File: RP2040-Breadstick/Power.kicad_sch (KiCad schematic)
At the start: 11 parts, among them IC501 LM66200DRLR, U501 AP2112K-3.3TRG1

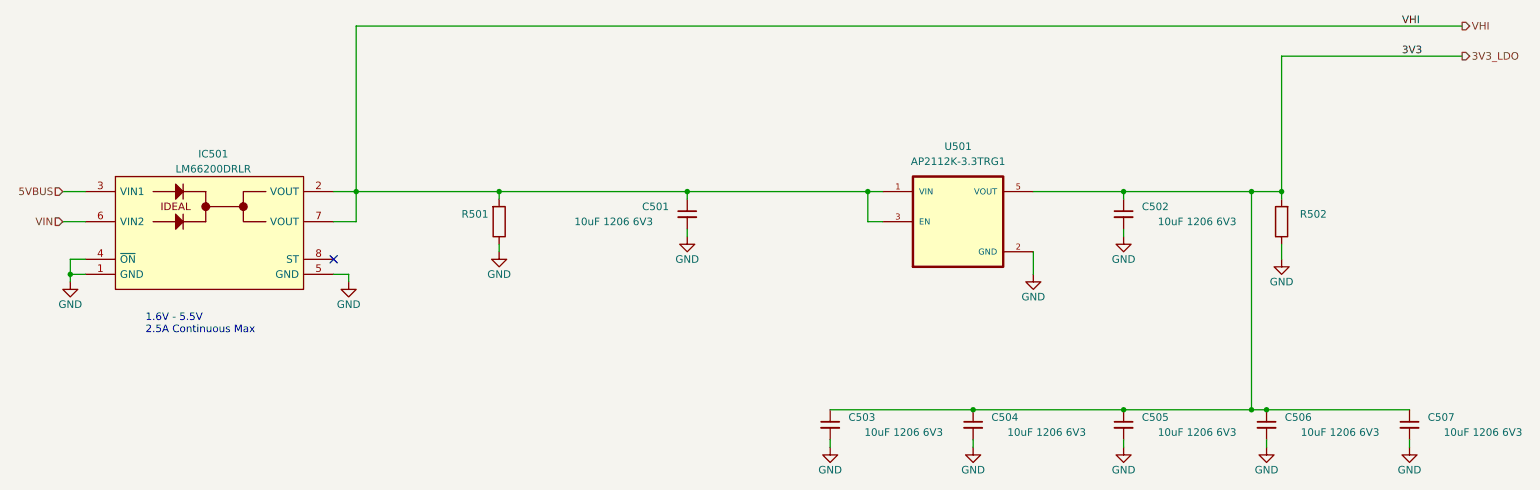
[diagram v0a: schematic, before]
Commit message: Rough routing complete, time to polish it a bit
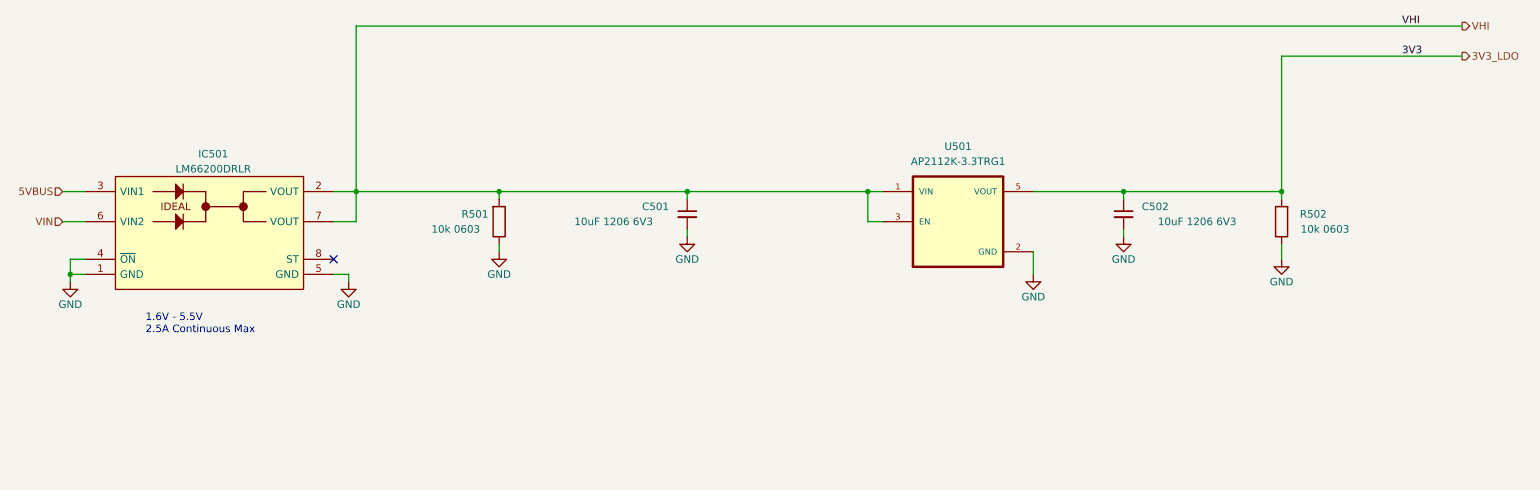
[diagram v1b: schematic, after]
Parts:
- removed C503, C504, C505, C506, C507: 10uF 1206 6V3, Capacitor_SMD:C_1206_3216Metric, symbol Device:C_Small
- R501: value (none) -> 10k 0603; footprint (none) -> Resistor_SMD:R_0603_1608Metric
- R502: value (none) -> 10k 0603

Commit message: Updated BOM
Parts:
- C501, C502: value 10uF 1206 6V3 -> (none); footprint Capacitor_SMD:C_1206_3216Metric -> (none)
- IC501: value LM66200DRLR -> (none); footprint SOTFL50P160X60-8L -> (none); Digikey (none) -> 296-LM66200DRLRCT-ND; Manufacturer (none) -> Texas Instruments; Mouser (none) -> 595-LM66200DRLR
- R501, R502: value 10k 0603 -> (none); footprint Resistor_SMD:R_0603_1608Metric -> (none)
- U501: value AP2112K-3.3TRG1 -> (none); footprint AP2112K-3:SOT95P285X140-5N -> (none); DigiKey_Part_Number AP2112K-3.3TRG1DITR-ND -> (none); Digikey (none) -> AP2112K-3.3TRG1DICT-ND; Manufacturer (none) -> Diodes Incorporated; Manufacturer_Part_Number (none) -> AP2112K-3.3TRG1; Mouser (none) -> 621-AP2112K-3.3TRG1; Package SOT-753 Diodes Inc. -> SOT-25
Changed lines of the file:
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@@
       (effects (font (size 1.27 1.27)) (justify left))
     )
-    (property "Value" "10k 0603" (id 1) (at 245.11 82.55 0)
-      (effects (font (size 1.27 1.27)) (justify left))
-    )
-    (property "Footprint" "Resistor_SMD:R_0603_1608Metric" (id 2) (at 235.458 81.28 90)
+    (property "Value" "" (id 1) (at 245.11 82.55 0)
+      (effects (font (size 1.27 1.27)) (justify left))
+    )
+    (property "Footprint" "" (id 2) (at 235.458 81.28 90)
       (effects (font (size 1.27 1.27)) hide)
     )
@@
       (effects (font (size 1.27 1.27)) (justify left))
     )
-    (property "Value" "10uF 1206 6V3" (id 1) (at 226.06 81.28 0)
-      (effects (font (size 1.27 1.27)) (justify left))
-    )
-    (property "Footprint" "Capacitor_SMD:C_1206_3216Metric" (id 2) (at 207.01 80.01 0)
+    (property "Value" "" (id 1) (at 226.06 81.28 0)
+      (effects (font (size 1.27 1.27)) (justify left))
+    )
+    (property "Footprint" "" (id 2) (at 207.01 80.01 0)
       (effects (font (size 1.27 1.27)) hide)
     )
@@
     (in_bom yes) (on_board yes)
     (property "Reference" "IC501" (id 0) (at 53.34 69.85 0))
-    (property "Value" "LM66200DRLR" (id 1) (at 53.34 72.39 0))
-    (property "Footprint" "SOTFL50P160X60-8L" (id 2) (at 82.55 81.28 0)
+    (property "Value" "" (id 1) (at 53.34 72.39 0))
+    (property "Footprint" "" (id 2) (at 82.55 81.28 0)
       (effects (font (size 1.27 1.27)) (justify left) hide)
     )
@@
     (property "Manufacturer_Part_Number" "LM66200DRLR" (id 9) (at 82.55 99.06 0)
       (effects (font (size 1.27 1.27)) (justify left) hide)
+    )
+    (property "Manufacturer" "Texas Instruments" (id 10) (at 53.34 83.82 0)
+      (effects (font (size 1.27 1.27)) hide)
+    )
+    (property "Digikey" "296-LM66200DRLRCT-ND" (id 11) (at 53.34 83.82 0)
+      (effects (font (size 1.27 1.27)) hide)
+    )
+    (property "Mouser" "595-LM66200DRLR" (id 12) (at 53.34 83.82 0)
+      (effects (font (size 1.27 1.27)) hide)
     )
     (pin "1")
@@
       (effects (font (size 1.27 1.27)) (justify left))
     )
-    (property "Value" "10uF 1206 6V3" (id 1) (at 114.3 81.28 0)
-      (effects (font (size 1.27 1.27)) (justify left))
-    )
-    (property "Footprint" "Capacitor_SMD:C_1206_3216Metric" (id 2) (at 133.35 80.01 0)
+    (property "Value" "" (id 1) (at 114.3 81.28 0)
+      (effects (font (size 1.27 1.27)) (justify left))
+    )
+    (property "Footprint" "" (id 2) (at 133.35 80.01 0)
       (effects (font (size 1.27 1.27)) hide)
     )
@@
     (in_bom yes) (on_board yes) (fields_autoplaced)
     (property "Reference" "U501" (id 0) (at 179.07 68.58 0))
-    (property "Value" "AP2112K-3.3TRG1" (id 1) (at 179.07 71.12 0))
-    (property "Footprint" "AP2112K-3:SOT95P285X140-5N" (id 2) (at 179.07 81.28 0)
+    (property "Value" "" (id 1) (at 179.07 71.12 0))
+    (property "Footprint" "" (id 2) (at 179.07 81.28 0)
       (effects (font (size 1.27 1.27)) (justify bottom) hide)
     )
@@
       (effects (font (size 1.27 1.27)) hide)
     )
-    (property "DigiKey_Part_Number" "AP2112K-3.3TRG1DITR-ND" (id 4) (at 179.07 81.28 0)
+    (property "DigiKey_Part_Number" "" (id 4) (at 179.07 81.28 0)
       (effects (font (size 1.27 1.27)) (justify bottom) hide)
     )
@@
       (effects (font (size 1.27 1.27)) (justify bottom) hide)
     )
-    (property "Package" "SOT-753 Diodes Inc." (id 7) (at 179.07 81.28 0)
+    (property "Package" "SOT-25" (id 7) (at 179.07 81.28 0)
       (effects (font (size 1.27 1.27)) (justify bottom) hide)
     )
@@
     (property "MANUFACTURER" "Diodes Inc." (id 13) (at 179.07 81.28 0)
       (effects (font (size 1.27 1.27)) (justify bottom) hide)
+    )
+    (property "Digikey" "AP2112K-3.3TRG1DICT-ND" (id 14) (at 179.07 81.28 0)
+      (effects (font (size 1.27 1.27)) hide)
+    )
+    (property "Manufacturer" "Diodes Incorporated" (id 15) (at 179.07 81.28 0)
+      (effects (font (size 1.27 1.27)) hide)
+    )
+    (property "Manufacturer_Part_Number" "AP2112K-3.3TRG1" (id 16) (at 179.07 81.28 0)
+      (effects (font (size 1.27 1.27)) hide)
+    )
+    (property "Mouser" "621-AP2112K-3.3TRG1" (id 17) (at 179.07 81.28 0)
+      (effects (font (size 1.27 1.27)) hide)
     )
     (pin "1")
@@
       (effects (font (size 1.27 1.27)) (justify left))
     )
-    (property "Value" "10k 0603" (id 1) (at 90.17 82.55 0)
-      (effects (font (size 1.27 1.27)) (justify left))
-    )
-    (property "Footprint" "Resistor_SMD:R_0603_1608Metric" (id 2) (at 99.822 81.28 90)
-      (effects (font (size 1.27 1.27)) hide)
-    )
+    (property "Value" "" (id 1) (at 90.17 82.55 0)
+      (effects (font (size 1.27 1.27)) (justify left))
+    )
+    (property "Footprint" "" (id 2) (at 99.822 81.28 90)
+      (effects (font (size 1.27 1.27)) hide)
+    )

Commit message: Continued fleshing out the BOM
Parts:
- removed C501, C502: (no value), symbol Device:C_Small
- added C501, C502: (no value), symbol Device:C_Polarized
- IC501: Package (none) -> SOT-583
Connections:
- net 3V3_LDO: now also C502.1
- net GND: now also C501.2, C502.2
- net VHI: now also C501.1
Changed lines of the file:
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@@
   (junction (at 101.6 76.2) (diameter 0) (color 0 0 0 0)
   )
+  (junction (at 201.93 76.2) (diameter 0) (color 0 0 0 0)
+  )
   (junction (at 29.21 90.17) (diameter 0) (color 0 0 0 0)
   )
@@
   (junction (at 233.68 76.2) (diameter 0) (color 0 0 0 0)
   )
-  (junction (at 207.01 76.2) (diameter 0) (color 0 0 0 0)
-  )
-  (junction (at 133.35 76.2) (diameter 0) (color 0 0 0 0)
+  (junction (at 132.08 76.2) (diameter 0) (color 0 0 0 0)
   )
   (no_connect (at 73.66 87.63))
@@
     (stroke (width 0) (type default) (color 0 0 0 0))
   )
-  (wire (pts (xy 133.35 76.2) (xy 163.83 76.2))
-    (stroke (width 0) (type default) (color 0 0 0 0))
-  )
   (wire (pts (xy 264.16 53.34) (xy 233.68 53.34))
     (stroke (width 0) (type default) (color 0 0 0 0))
   )
-  (wire (pts (xy 207.01 82.55) (xy 207.01 83.82))
-    (stroke (width 0) (type default) (color 0 0 0 0))
-  )
   (wire (pts (xy 163.83 81.28) (xy 166.37 81.28))
     (stroke (width 0) (type default) (color 0 0 0 0))
   )
-  (wire (pts (xy 133.35 82.55) (xy 133.35 83.82))
-    (stroke (width 0) (type default) (color 0 0 0 0))
-  )
-  (wire (pts (xy 207.01 76.2) (xy 207.01 77.47))
+  (wire (pts (xy 201.93 76.2) (xy 201.93 77.47))
     (stroke (width 0) (type default) (color 0 0 0 0))
   )
@@
     (stroke (width 0) (type default) (color 0 0 0 0))
   )
-  (wire (pts (xy 207.01 76.2) (xy 233.68 76.2))
-    (stroke (width 0) (type default) (color 0 0 0 0))
-  )
   (wire (pts (xy 233.68 76.2) (xy 233.68 77.47))
     (stroke (width 0) (type default) (color 0 0 0 0))
@@
     (stroke (width 0) (type default) (color 0 0 0 0))
   )
-  (wire (pts (xy 191.77 76.2) (xy 207.01 76.2))
+  (wire (pts (xy 132.08 76.2) (xy 132.08 77.47))
+    (stroke (width 0) (type default) (color 0 0 0 0))
+  )
+  (wire (pts (xy 191.77 76.2) (xy 201.93 76.2))
     (stroke (width 0) (type default) (color 0 0 0 0))
   )
@@
     (stroke (width 0) (type default) (color 0 0 0 0))
   )
+  (wire (pts (xy 132.08 85.09) (xy 132.08 86.36))
+    (stroke (width 0) (type default) (color 0 0 0 0))
+  )
+  (wire (pts (xy 201.93 85.09) (xy 201.93 86.36))
+    (stroke (width 0) (type default) (color 0 0 0 0))
+  )
   (wire (pts (xy 73.66 90.17) (xy 76.2 90.17))
     (stroke (width 0) (type default) (color 0 0 0 0))
@@
     (stroke (width 0) (type default) (color 0 0 0 0))
   )
+  (wire (pts (xy 201.93 76.2) (xy 233.68 76.2))
+    (stroke (width 0) (type default) (color 0 0 0 0))
+  )
   (wire (pts (xy 77.47 48.26) (xy 77.47 76.2))
     (stroke (width 0) (type default) (color 0 0 0 0))
@@
     (stroke (width 0) (type default) (color 0 0 0 0))
   )
-  (wire (pts (xy 133.35 76.2) (xy 133.35 77.47))
-    (stroke (width 0) (type default) (color 0 0 0 0))
-  )
-  (wire (pts (xy 101.6 76.2) (xy 133.35 76.2))
+  (wire (pts (xy 101.6 76.2) (xy 132.08 76.2))
+    (stroke (width 0) (type default) (color 0 0 0 0))
+  )
+  (wire (pts (xy 132.08 76.2) (xy 163.83 76.2))
     (stroke (width 0) (type default) (color 0 0 0 0))
   )
@@
     )
     (pin "1")
-  )
-  (symbol (lib_id "Device:C_Small") (at 207.01 80.01 0) (mirror y) (unit 1)
-    (in_bom yes) (on_board yes)
-    (property "Reference" "C502" (id 0) (at 214.63 78.74 0)
-      (effects (font (size 1.27 1.27)) (justify left))
-    )
-    (property "Value" "" (id 1) (at 226.06 81.28 0)
-      (effects (font (size 1.27 1.27)) (justify left))
-    )
-    (property "Footprint" "" (id 2) (at 207.01 80.01 0)
-      (effects (font (size 1.27 1.27)) hide)
-    )
-    (property "Datasheet" "~" (id 3) (at 207.01 80.01 0)
-      (effects (font (size 1.27 1.27)) hide)
-    )
-    (property "JLCPCB P/N" "" (id 4) (at 207.01 80.01 0)
-      (effects (font (size 1.27 1.27)) hide)
-    )
-    (property "Digikey" "1276-1134-6-ND" (id 5) (at 207.01 80.01 0)
-      (effects (font (size 1.27 1.27)) hide)
-    )
-    (pin "1")
-    (pin "2")
   )
   (symbol (lib_id "LM66200DRLR:LM66200DRLR") (at 53.34 83.82 0) (unit 1)
@@
     )
     (property "Mouser" "595-LM66200DRLR" (id 12) (at 53.34 83.82 0)
+      (effects (font (size 1.27 1.27)) hide)
+    )
+    (property "Package" "SOT-583" (id 13) (at 53.34 83.82 0)
       (effects (font (size 1.27 1.27)) hide)
     )
@@
     (pin "8")
   )
+  (symbol (lib_id "Device:C_Polarized") (at 201.93 81.28 0) (unit 1)
+    (in_bom yes) (on_board yes) (fields_autoplaced)
+    (property "Reference" "C502" (id 0) (at 205.74 79.1209 0)
+      (effects (font (size 1.27 1.27)) (justify left))
+    )
+    (property "Value" "" (id 1) (at 205.74 81.6609 0)
+      (effects (font (size 1.27 1.27)) (justify left))
+    )
+    (property "Footprint" "" (id 2) (at 202.8952 85.09 0)
+      (effects (font (size 1.27 1.27)) hide)
+    )
+    (property "Datasheet" "~" (id 3) (at 201.93 81.28 0)
+      (effects (font (size 1.27 1.27)) hide)
+    )
+    (property "Digikey" "399-3684-1-ND" (id 4) (at 201.93 81.28 0)
+      (effects (font (size 1.27 1.27)) hide)
+    )
+    (property "Manufacturer" "KEMET" (id 5) (at 201.93 81.28 0)
+      (effects (font (size 1.27 1.27)) hide)
+    )
+    (property "Manufacturer_Part_Number" "T491A106K010AT" (id 6) (at 201.93 81.28 0)
+      (effects (font (size 1.27 1.27)) hide)
+    )
+    (property "Mouser" "80-T491A106K010" (id 7) (at 201.93 81.28 0)
+      (effects (font (size 1.27 1.27)) hide)
+    )
+    (property "Package" "1206" (id 8) (at 201.93 81.28 0)
+      (effects (font (size 1.27 1.27)) hide)
+    )
+    (pin "1")
+    (pin "2")
+  )
+  (symbol (lib_id "power:GND") (at 201.93 86.36 0) (unit 1)
+    (in_bom yes) (on_board yes)
+    (property "Reference" "#PWR0506" (id 0) (at 201.93 92.71 0)
+      (effects (font (size 1.27 1.27)) hide)
+    )
+    (property "Value" "GND" (id 1) (at 201.93 90.17 0))
+    (property "Footprint" "" (id 2) (at 201.93 86.36 0)
+      (effects (font (size 1.27 1.27)) hide)
+    )
+    (property "Datasheet" "" (id 3) (at 201.93 86.36 0)
+      (effects (font (size 1.27 1.27)) hide)
+    )
+    (pin "1")
+  )
   (symbol (lib_id "power:GND") (at 101.6 86.36 0) (unit 1)
     (in_bom yes) (on_board yes)
@@
     (pin "1")
   )
-  (symbol (lib_id "Device:C_Small") (at 133.35 80.01 0) (unit 1)
-    (in_bom yes) (on_board yes)
-    (property "Reference" "C501" (id 0) (at 125.73 78.74 0)
-      (effects (font (size 1.27 1.27)) (justify left))
-    )
-    (property "Value" "" (id 1) (at 114.3 81.28 0)
-      (effects (font (size 1.27 1.27)) (justify left))
-    )
-    (property "Footprint" "" (id 2) (at 133.35 80.01 0)
-      (effects (font (size 1.27 1.27)) hide)
-    )
-    (property "Datasheet" "~" (id 3) (at 133.35 80.01 0)
-      (effects (font (size 1.27 1.27)) hide)
-    )
-    (property "JLCPCB P/N" "" (id 4) (at 133.35 80.01 0)
-      (effects (font (size 1.27 1.27)) hide)
-    )
-    (property "Digikey" "1276-1134-6-ND" (id 5) (at 133.35 80.01 0)
-      (effects (font (size 1.27 1.27)) hide)
-    )
-    (pin "1")
-    (pin "2")
-  )
   (symbol (lib_id "power:GND") (at 76.2 91.44 0) (mirror y) (unit 1)
     (in_bom yes) (on_board yes)
@@
     )
     (pin "1")
+  )
+  (symbol (lib_id "Device:C_Polarized") (at 132.08 81.28 0) (unit 1)
+    (in_bom yes) (on_board yes) (fields_autoplaced)
+    (property "Reference" "C501" (id 0) (at 135.89 79.1209 0)
+      (effects (font (size 1.27 1.27)) (justify left))
+    )
+    (property "Value" "" (id 1) (at 135.89 81.6609 0)
+      (effects (font (size 1.27 1.27)) (justify left))
+    )
+    (property "Footprint" "" (id 2) (at 133.0452 85.09 0)
+      (effects (font (size 1.27 1.27)) hide)
+    )
+    (property "Datasheet" "~" (id 3) (at 132.08 81.28 0)
+      (effects (font (size 1.27 1.27)) hide)
+    )
+    (property "Digikey" "399-3684-1-ND" (id 4) (at 132.08 81.28 0)
+      (effects (font (size 1.27 1.27)) hide)
+    )
+    (property "Manufacturer" "KEMET" (id 5) (at 132.08 81.28 0)
+      (effects (font (size 1.27 1.27)) hide)
+    )
+    (property "Manufacturer_Part_Number" "T491A106K010AT" (id 6) (at 132.08 81.28 0)
+      (effects (font (size 1.27 1.27)) hide)
+    )
+    (property "Mouser" "80-T491A106K010" (id 7) (at 132.08 81.28 0)
+      (effects (font (size 1.27 1.27)) hide)
+    )
+    (property "Package" "1206" (id 8) (at 132.08 81.28 0)
+      (effects (font (size 1.27 1.27)) hide)
+    )
+    (pin "1")
+    (pin "2")
   )
   (symbol (lib_id "AP2112K-3.3TRG1:AP2112K-3.3TRG1") (at 179.07 81.28 0) (unit 1)
@@
     (pin "2")
   )
-  (symbol (lib_id "power:GND") (at 207.01 83.82 0) (mirror y) (unit 1)
-    (in_bom yes) (on_board yes)
-    (property "Reference" "#PWR0506" (id 0) (at 207.01 90.17 0)
-      (effects (font (size 1.27 1.27)) hide)
-    )
-    (property "Value" "GND" (id 1) (at 207.01 87.63 0))
-    (property "Footprint" "" (id 2) (at 207.01 83.82 0)
-      (effects (font (size 1.27 1.27)) hide)
-    )
-    (property "Datasheet" "" (id 3) (at 207.01 83.82 0)
-      (effects (font (size 1.27 1.27)) hide)
-    )
-    (pin "1")
-  )
-  (symbol (lib_id "power:GND") (at 133.35 83.82 0) (unit 1)
-    (in_bom yes) (on_board yes)
-    (property "Reference" "#PWR0504" (id 0) (at 133.35 90.17 0)
-      (effects (font (size 1.27 1.27)) hide)
-    )
-    (property "Value" "GND" (id 1) (at 133.35 87.63 0))
-    (property "Footprint" "" (id 2) (at 133.35 83.82 0)
-      (effects (font (size 1.27 1.27)) hide)
-    )
-    (property "Datasheet" "" (id 3) (at 133.35 83.82 0)
-      (effects (font (size 1.27 1.27)) hide)
-    )
+  (symbol (lib_id "power:GND") (at 132.08 86.36 0) (unit 1)
+    (in_bom yes) (on_board yes)
+    (property "Reference" "#PWR0504" (id 0) (at 132.08 92.71 0)
+      (effects (font (size 1.27 1.27)) hide)
+    )
+    (property "Value" "GND" (id 1) (at 132.08 90.17 0))
+    (property "Footprint" "" (id 2) (at 132.08 86.36 0)
+      (effects (font (size 1.27 1.27)) hide)
+    )
+    (property "Datasheet" "" (id 3) (at 132.08 86.36 0)
+      (effects (font (size 1.27 1.27)) hide)
+    )

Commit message: More BOM updates
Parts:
- R501, R502: Digikey P122413DKR-ND -> 311-10.0KHRCT-ND; Manufacturer (none) -> YAGEO; Manufacturer_Part_Number (none) -> RC0603FR-0710KL; Mouser (none) -> 603-RC0603FR-0710KL; Package (none) -> 0603
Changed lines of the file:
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@@
       (effects (font (size 1.27 1.27)) hide)
     )
-    (property "Digikey" "P122413DKR-ND" (id 5) (at 233.68 81.28 0)
+    (property "Digikey" "311-10.0KHRCT-ND" (id 5) (at 233.68 81.28 0)
+      (effects (font (size 1.27 1.27)) hide)
+    )
+    (property "Manufacturer" "YAGEO" (id 6) (at 233.68 81.28 0)
+      (effects (font (size 1.27 1.27)) hide)
+    )
+    (property "Manufacturer_Part_Number" "RC0603FR-0710KL" (id 7) (at 233.68 81.28 0)
+      (effects (font (size 1.27 1.27)) hide)
+    )
+    (property "Mouser" "603-RC0603FR-0710KL" (id 8) (at 233.68 81.28 0)
+      (effects (font (size 1.27 1.27)) hide)
+    )
+    (property "Package" "0603" (id 9) (at 233.68 81.28 0)
       (effects (font (size 1.27 1.27)) hide)
     )
@@
       (effects (font (size 1.27 1.27)) hide)
     )
-    (property "Digikey" "P122413DKR-ND" (id 5) (at 101.6 81.28 0)
-      (effects (font (size 1.27 1.27)) hide)
-    )
+    (property "Digikey" "311-10.0KHRCT-ND" (id 5) (at 101.6 81.28 0)
+      (effects (font (size 1.27 1.27)) hide)
+    )
+    (property "Manufacturer" "YAGEO" (id 6) (at 101.6 81.28 0)
+      (effects (font (size 1.27 1.27)) hide)
+    )
+    (property "Manufacturer_Part_Number" "RC0603FR-0710KL" (id 7) (at 101.6 81.28 0)
+      (effects (font (size 1.27 1.27)) hide)
+    )
+    (property "Mouser" "603-RC0603FR-0710KL" (id 8) (at 101.6 81.28 0)
+      (effects (font (size 1.27 1.27)) hide)
+    )
+    (property "Package" "0603" (id 9) (at 101.6 81.28 0)
+      (effects (font (size 1.27 1.27)) hide)
+    )
